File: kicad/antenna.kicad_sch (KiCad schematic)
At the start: 37 parts, among them J1 Bus_PCI_Express_x1, J4 Conn_01x02, J5 Conn_02x08_Odd_Even, J6 USB_C_Receptacle_USB2.0_16P, U2 RP2040, U4 W25Q128JVP, U9 MCP25625T-E/ML, X1 ABM8-272-T3, Y2 X322516MLB4SI

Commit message: update project to kicad 9, remove test label in title
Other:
- note added: "Antenna Module 0.1.0"
- note removed: "Antenna Module 0.1.0 test"
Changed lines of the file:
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@@
 (kicad_sch
-	(version 20231120)
+	(version 20250114)
 	(generator "eeschema")
-	(generator_version "8.0")
+	(generator_version "9.0")
 	(paper "A2")
+	(text "Make sure C210 is close to pin 44 of RP2040"
+		(exclude_from_sim no)
+		(at 326.39 125.73 0)
+		(effects
+			(font
+				(size 1.27 1.27)
+			)
+			(justify left bottom)
+		)
+	)
+	(text "Make sure C8 is close to pin 45 of RP2040"
+		(exclude_from_sim no)
+		(at 231.14 125.73 0)
+		(effects
+			(font
+				(size 1.27 1.27)
+			)
+			(justify left bottom)
+		)
+	)
+	(text "RP2040 Crystal"
+		(exclude_from_sim no)
+		(at 164.465 247.65 0)
+		(effects
+			(font
+				(size 2.54 2.54)
+			)
+			(justify left bottom)
+		)
+	)
+	(text "USB"
+		(exclude_from_sim no)
+		(at 111.252 53.34 0)
+		(effects
+			(font
+				(size 2.54 2.54)
+			)
+			(justify left bottom)
+		)
+	)
+	(text "Make sure R3 and R4 are close to RP2040"
+		(exclude_from_sim no)
+		(at 261.62 142.494 0)
+		(effects
+			(font
+				(size 1.27 1.27)
+			)
+			(justify right bottom)
+		)
+	)
+	(text "CAN"
+		(exclude_from_sim no)
+		(at 338.836 197.612 0)
+		(effects
+			(font
+				(size 1.524 1.524)
+			)
+			(justify left bottom)
+		)
+	)
+	(text "RFD"
+		(exclude_from_sim no)
+		(at 333.756 148.336 0)
+		(effects
+			(font
+				(size 1.524 1.524)
+			)
+			(justify left bottom)
+		)
+	)
+	(text "USB Boot \nshorting headders"
+		(exclude_from_sim no)
+		(at 46.99 155.448 0)
+		(effects
+			(font
+				(size 2.54 2.54)
+			)
+			(justify left bottom)
+		)
+	)
+	(text "Antenna Module 0.1.0"
+		(exclude_from_sim no)
+		(at 493.014 386.842 0)
+		(effects
+			(font
+				(size 4 4)
+			)
+			(justify left bottom)
+		)
+	)
+	(text "Gold Fingers"
+		(exclude_from_sim no)
+		(at 65.532 260.096 0)
+		(effects
+			(font
+				(size 2.54 2.54)
+			)
+			(justify left bottom)
+		)
+	)
+	(text "MCU"
+		(exclude_from_sim no)
+		(at 297.18 186.436 0)
+		(effects
+			(font
+				(size 2.54 2.54)
+			)
+			(justify left bottom)
+		)
+	)
+	(text "CAN Controller/Tranceiver"
+		(exclude_from_sim no)
+		(at 270.002 314.96 0)
+		(effects
+			(font
+				(size 2.54 2.54)
+			)
+			(justify left bottom)
+		)
+	)
+	(text "Flash"
+		(exclude_from_sim no)
+		(at 119.38 159.512 0)
+		(effects
+			(font
+				(size 2.54 2.54)
+			)
+			(justify left bottom)
+		)
+	)
 	(junction
 		(at 252.73 334.01)
@@
 		)
 	)
-	(text "Make sure C210 is close to pin 44 of RP2040"
-		(exclude_from_sim no)
-		(at 326.39 125.73 0)
-		(effects
-			(font
-				(size 1.27 1.27)
-			)
-			(justify left bottom)
-		)
-	)
-	(text "Make sure C8 is close to pin 45 of RP2040"
-		(exclude_from_sim no)
-		(at 231.14 125.73 0)
-		(effects
-			(font
-				(size 1.27 1.27)
-			)
-			(justify left bottom)
-		)
-	)
-	(text "RP2040 Crystal"
-		(exclude_from_sim no)
-		(at 164.465 247.65 0)
-		(effects
-			(font
-				(size 2.54 2.54)
-			)
-			(justify left bottom)
-		)
-	)
-	(text "USB"
-		(exclude_from_sim no)
-		(at 111.252 53.34 0)
-		(effects
-			(font
-				(size 2.54 2.54)
-			)
-			(justify left bottom)
-		)
-	)
-	(text "Make sure R3 and R4 are close to RP2040"
-		(exclude_from_sim no)
-		(at 261.62 142.494 0)
-		(effects
-			(font
-				(size 1.27 1.27)
-			)
-			(justify right bottom)
-		)
-	)
-	(text "CAN"
-		(exclude_from_sim no)
-		(at 338.836 197.612 0)
-		(effects
-			(font
-				(size 1.524 1.524)
-			)
-			(justify left bottom)
-		)
-	)
-	(text "RFD"
-		(exclude_from_sim no)
-		(at 333.756 148.336 0)
-		(effects
-			(font
-				(size 1.524 1.524)
-			)
-			(justify left bottom)
-		)
-	)
-	(text "USB Boot \nshorting headders"
-		(exclude_from_sim no)
-		(at 46.99 155.448 0)
-		(effects
-			(font
-				(size 2.54 2.54)
-			)
-			(justify left bottom)
-		)
-	)
-	(text "Antenna Module 0.1.0 test"
-		(exclude_from_sim no)
-		(at 493.014 386.842 0)
-		(effects
-			(font
-				(size 4 4)
-			)
-			(justify left bottom)
-		)
-	)
-	(text "Gold Fingers"
-		(exclude_from_sim no)
-		(at 65.532 260.096 0)
-		(effects
-			(font
-				(size 2.54 2.54)
-			)
-			(justify left bottom)
-		)
-	)
-	(text "MCU"
-		(exclude_from_sim no)
-		(at 297.18 186.436 0)
-		(effects
-			(font
-				(size 2.54 2.54)
-			)
-			(justify left bottom)
-		)
-	)
-	(text "CAN Controller/Tranceiver"
-		(exclude_from_sim no)
-		(at 270.002 314.96 0)
-		(effects
-			(font
-				(size 2.54 2.54)
-			)
-			(justify left bottom)
-		)
-	)
-	(text "Flash"
-		(exclude_from_sim no)
-		(at 119.38 159.512 0)
-		(effects
-			(font
-				(size 2.54 2.54)
-			)
-			(justify left bottom)
-		)
-	)
 	(label "USB_D2+"
 		(at 262.89 151.13 0)
@@
 		)
 	)
+	(embedded_fonts no)
 )

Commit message: create RFD900 footprint, update schematic library to global
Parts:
- removed J4: Conn_01x02, Connector_PinHeader_2.54mm:PinHeader_1x02_P2.54mm_Vertical, symbol Connector_Generic:Conn_01x02
- removed J5: Conn_02x08_Odd_Even, Connector_PinSocket_2.54mm:PinSocket_2x08_P2.54mm_Vertical, symbol Connector_Generic:Conn_02x08_Odd_Even
- removed S1, S2: TS-1187A-B-A-B, TS-1187A-B-A-B:SW_TS-1187A-B-A-B, symbol TS-1187A-B-A-B:TS-1187A-B-A-B
- removed U9: MCP25625T-E/ML, MCP25625T_E_ML:QFN28_6X6MC_MCH, symbol MCP25625:MCP25625T-E_ML
- removed X1: ABM8-272-T3, ABM8-272-T3:ABM8-272-T3_ABR, symbol crystal:ABM8-272-T3
- removed Y2: X322516MLB4SI, X322516MLB4SI:OSC_X322516MLB4SI, symbol X322516MLB4SI:X322516MLB4SI
- added J2: Conn_01x04, Connector:NS-Tech_Grove_1x04_P2mm_Vertical, symbol Connector_Generic:Conn_01x04
- added J5: Conn_01x02, Connector_PinHeader_2.54mm:PinHeader_1x02_P2.54mm_Vertical, symbol Connector_Generic:Conn_01x02
- added S2: TS-1187A-B-A-B, 4in-kicad-library:TS-1187A-B-A-B, symbol 4in-kicad-library:TS-1187A-B-A-B
- added U1: RFD900, 4in-antenna:RFD900, symbol 4in-antenna:RFD900
- added U9: MCP25625T-E/ML, 4in-kicad-library:QFN28_6X6MC_MCH, symbol 4in-kicad-library:MCP25625T-E_ML
- added X1: RP2040 Crystal, 4in-kicad-library:ABM8-272-T3_ABR, symbol 4in-kicad-library:ABM8-272-T3
- added Y2: X322516MLB4SI, 4in-kicad-library:X322516MLB4SI, symbol 4in-kicad-library:X322516MLB4SI
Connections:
- net +3.3V: now also J2.3 (Pin_3), U9.11 (VIO), U9.3 (VDD)
- net +5V: now also U1.4 (Vcc), U9.19 (VDDA)
- net CANINT: now also U9.25 (*INT)
- net CANN: now also U9.12 (CANL)
- net CANP: now also U9.13 (CANH)
- net CANRESET: now also U9.2 (*RESET)
- net CANSTBY: now also U9.15 (STBY)
- net CS: now also U9.1 (*CS)
- net CTS: now also U1.3 (CTS)
- net GND: now also J2.4 (Pin_4), J5.2 (Pin_2), S2.A, S2.B, U1.1 (GND), U1.16 (GND), U1.2 (GND), U9.18 (VSS), U9.22 (GND), U9.29 (EPAD), X1.2, X1.4, Y2.2, Y2.4
- net OSC1: now also U9.21 (OSC1), Y2.1
- net OSC2: now also U9.20 (OSC2), Y2.3
- net P1.0: now also U1.13 (P0.1)
- net P1.1: now also U1.15 (P2.6)
- net P1.2: now also U1.14 (P2.0)
- net P1.3: now also U1.12 (P2.1)
- net P3.3: now also U1.10 (P2.2)
- net P3.4: now also U1.8 (P2.3)
- net RTS: now also U1.11 (RTS)
- net RUN: now also S2.C, S2.D
- net RX: now also U1.7 (RX)
- net SCK: now also U9.26 (SCK)
- net SI: now also U9.27 (SI)
- net SO: now also U9.28 (SO)
- net SWCLK: now also J2.1 (Pin_1)
- net SWD: now also J2.2 (Pin_2)
- net TX: now also U1.9 (TX)
- net Vusb: now also U1.5 (Vusb), U1.6 (Vusb)
- net XIN: now also X1.1
- net XOUT_pre: now also X1.3
- net rx: now also U9.10 (RXD), U9.5 (RXCAN)
- net tx: now also U9.16 (TXD), U9.4 (TXCAN)
- net ~{USB_BOOT_S}: now also J5.1 (Pin_1)

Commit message: route USB, add LED
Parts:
- added D1: LED, LED_SMD:LED_0603_1608Metric, symbol Device:LED
- added R1: 1.5k, Resistor_SMD:R_0603_1608Metric, symbol Device:R
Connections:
- net +3.3V: now also D1.2 (A)
- net GND: now also R1.2
- net Vusb: no longer names the net of U1.5 (Vusb)
- net Vusb: no longer U1.6 (Vusb)
- new net: D1.1 (K), R1.1
- no-connect marks 31 -> 33
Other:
- note added: "Antenna Module 0.1.1"
- note removed: "Antenna Module 0.1.0"

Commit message: finalize version 0.1.1 for ordering
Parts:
- C10, C11: LCSC PN (none) -> C1548
- C206, C207, C209, C211, C212, C213, C214, C215, C216, C40, C90, C92, C93: LCSC PN (none) -> C307331
- C208, C210: LCSC PN (none) -> C52923
- C94, C95: LCSC PN (none) -> C1555
- D1: LCSC PN (none) -> C2286
- J1, J5: LCSC PN (none) -> n/a
- J2, U1: JLC Link (none) -> n/a; LCSC PN (none) -> n/a; LCSC Part # (none) -> n/a; now not fitted
- J6: LCSC PN (none) -> C2765186
- R1: LCSC PN (none) -> C22808
- R12, R30: LCSC PN (none) -> C11702
- R203, R204: LCSC PN (none) -> C25100
- R3, R4: LCSC PN (none) -> C25905
- R91: LCSC PN (none) -> C25744
- S2: LCSC Part # (none) -> C318884
- U2: LCSC PN (none) -> C2040
- U4: LCSC PN (none) -> C190862
- U9: LCSC Part # (none) -> C191253
- X1: LCSC Part # (none) -> C20625731
- Y2: LCSC Part # (none) -> C12668
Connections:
- net RX_rfd: now reaches U2.11 (GPIO8)
- net RX_rfd: now also U1.7 (RX)
- net CTS renamed CTS_rfd
- net P1.0: no longer names the net of U1.13 (P0.1)
- net P1.1: no longer names the net of U1.15 (P2.6)
- net P1.2: no longer names the net of U1.14 (P2.0)
- net P1.3: no longer names the net of U1.12 (P2.1)
- net P3.3: no longer names the net of U1.10 (P2.2)
- net P3.4: no longer names the net of U1.8 (P2.3)
- net RTS renamed RTS_rfd
- net RTS_rfd: now also U2.8 (GPIO6); no longer U2.7 (GPIO5)
- removed net RX: U1.7 (RX), U2.8 (GPIO6)
- net TX: no longer names the net of U2.5 (GPIO3)
- net TX: no longer U1.9 (TX)
- new net TX_rfd: U1.9 (TX), U2.7 (GPIO5)
- no-connect marks 33 -> 47
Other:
- note added: "RFD900"
- note removed: "RFD"

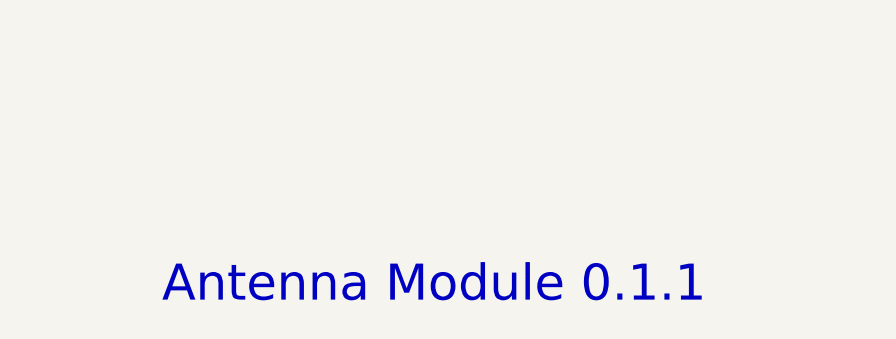
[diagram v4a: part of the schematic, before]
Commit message: move flash away from mounting hole, update to text to 0.2.0
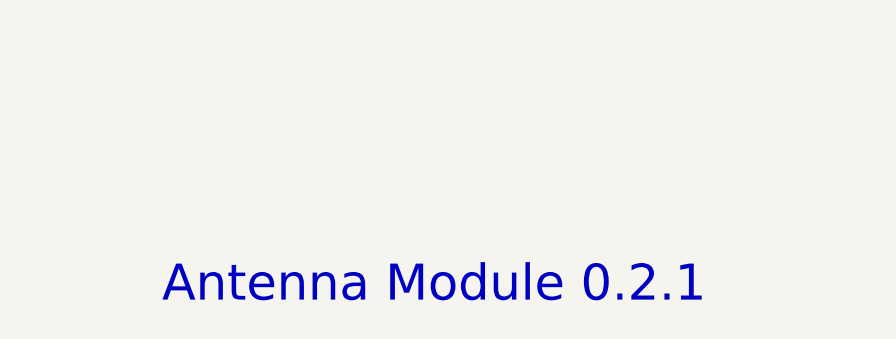
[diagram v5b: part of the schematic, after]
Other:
- note added: "Antenna Module 0.2.1"
- note removed: "Antenna Module 0.1.1"
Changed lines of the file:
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@@
 		)
 	)
-	(text "Antenna Module 0.1.1"
+	(text "Antenna Module 0.2.1"
 		(exclude_from_sim no)
 		(at 493.014 386.842 0)

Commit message: export final production files for 0.2.0
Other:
- note added: "Antenna Module 0.2.0"
- note removed: "Antenna Module 0.2.1"
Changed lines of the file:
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@@
 		)
 	)
-	(text "Antenna Module 0.2.1"
+	(text "Antenna Module 0.2.0"
 		(exclude_from_sim no)
 		(at 493.014 386.842 0)
